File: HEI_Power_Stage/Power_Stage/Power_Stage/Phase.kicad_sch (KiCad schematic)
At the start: 31 parts, among them IC1 ACS730KLCTR-65ABT, Q1 EPC2304ENGRT, Q2 EPC2304ENGRT, U2 MP18831-4AGY

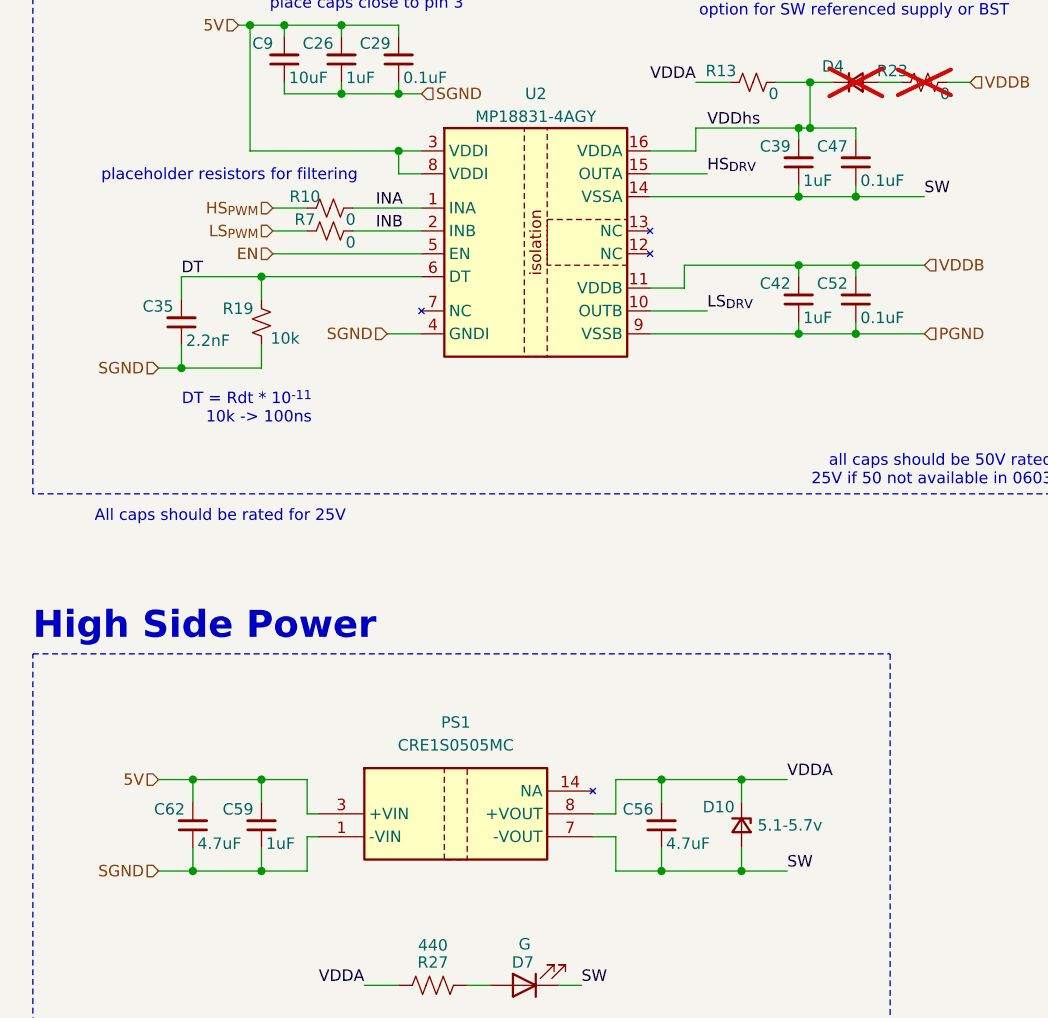
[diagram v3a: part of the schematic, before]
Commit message: placement rough draft
roughly placed all components
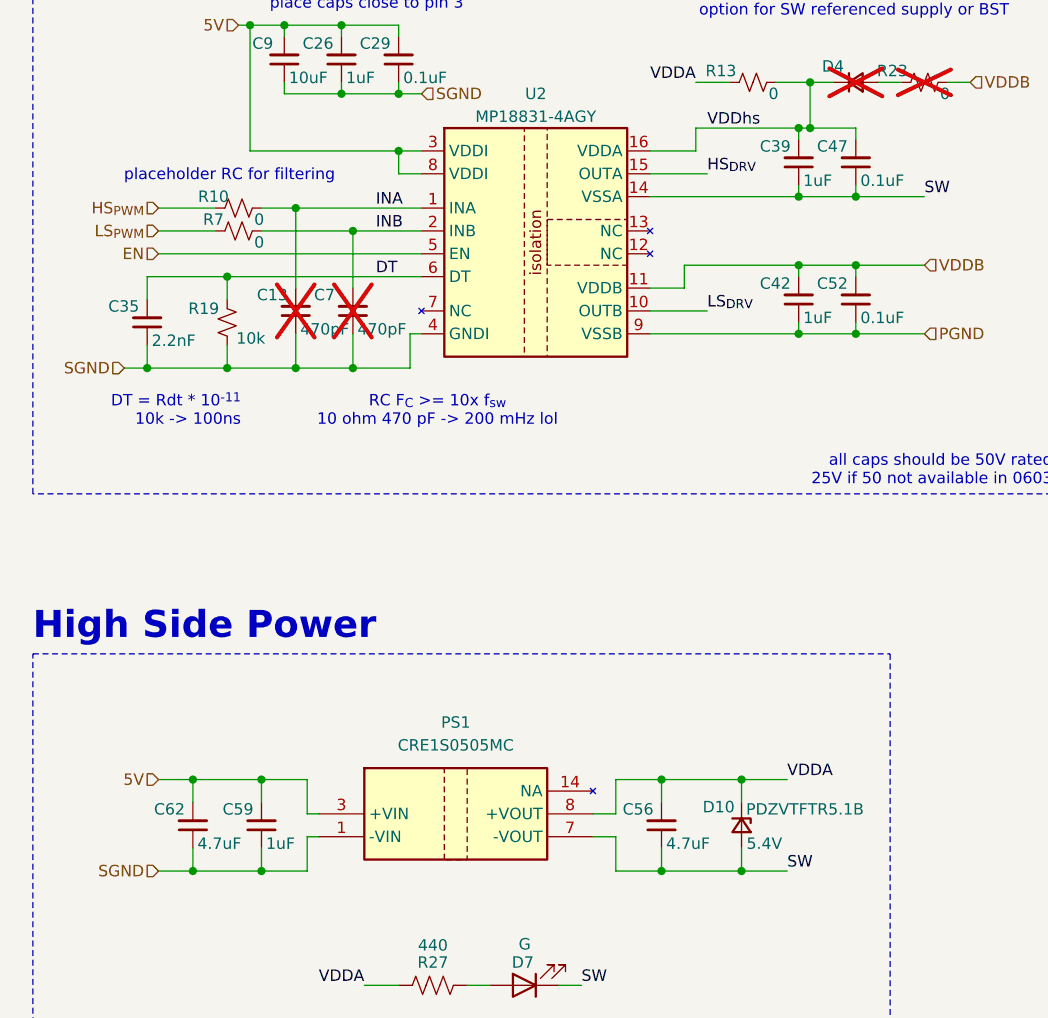
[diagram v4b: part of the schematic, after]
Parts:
- added C13, C7: 470pF, Capacitor_SMD:C_0603_1608Metric_Pad1.08x0.95mm_HandSolder, symbol Device:C_Small
- D10: value 5.1-5.7v -> PDZVTFTR5.1B; Vbreakdown (none) -> 5.4V
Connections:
- net INA: now also C13.2
- net INB: now also C7.2
- net SGND: now also C13.1, C7.1
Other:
- note added: "RC F_{C} >= 10x f_{sw} 10 ohm 470 pF -> 200 mHz lol"
- note added: "placeholder RC for filtering"
- note removed: "All caps should be rated for 25V"
- note removed: "placeholder resistors for filtering"
- moved on the sheet: C35, R10, R19, R7

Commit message: some change
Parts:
- added D13, D22: PDZVTFTR5.1B, Diode_SMD:D_SOD-128, symbol Device:D_Zener_Small
- added D14, D19: 300mV 1A, Diode_SMD:D_SOD-123F, symbol Device:D_Schottky_Small
- added R31, R5: 0, Resistor_SMD:R_0603_1608Metric_Pad0.98x0.95mm_HandSolder, symbol Device:R_Small_US
- D4: value ~ -> 300mV 1A; footprint Diode_SMD:D_SOD-523 -> Diode_SMD:D_SOD-123F; symbol Device:D_Small -> Device:D_Schottky_Small
- R23: footprint LED_SMD:LED_0603_1608Metric_Pad1.05x0.95mm_HandSolder -> Resistor_SMD:R_0603_1608Metric_Pad0.98x0.95mm_HandSolder
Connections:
- net HS_{DRV}: now also R5.1
- net HS_{Gate}: now also D14.2 (A), D22.1 (K)
- net LS_{DRV}: now also R31.1
- net LS_{Gate}: now also D13.1 (K), D19.2 (A)
- net PGND: now also D13.2 (A)
- net SW: now also D22.2 (A)
- new net: D14.1 (K), R5.2
- new net: D19.1 (K), R31.2
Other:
- note added: "zener on output of regulator to limit voltage into VDDx or on output of driver to limit directly into gate"
- moved on the sheet: R14, R4

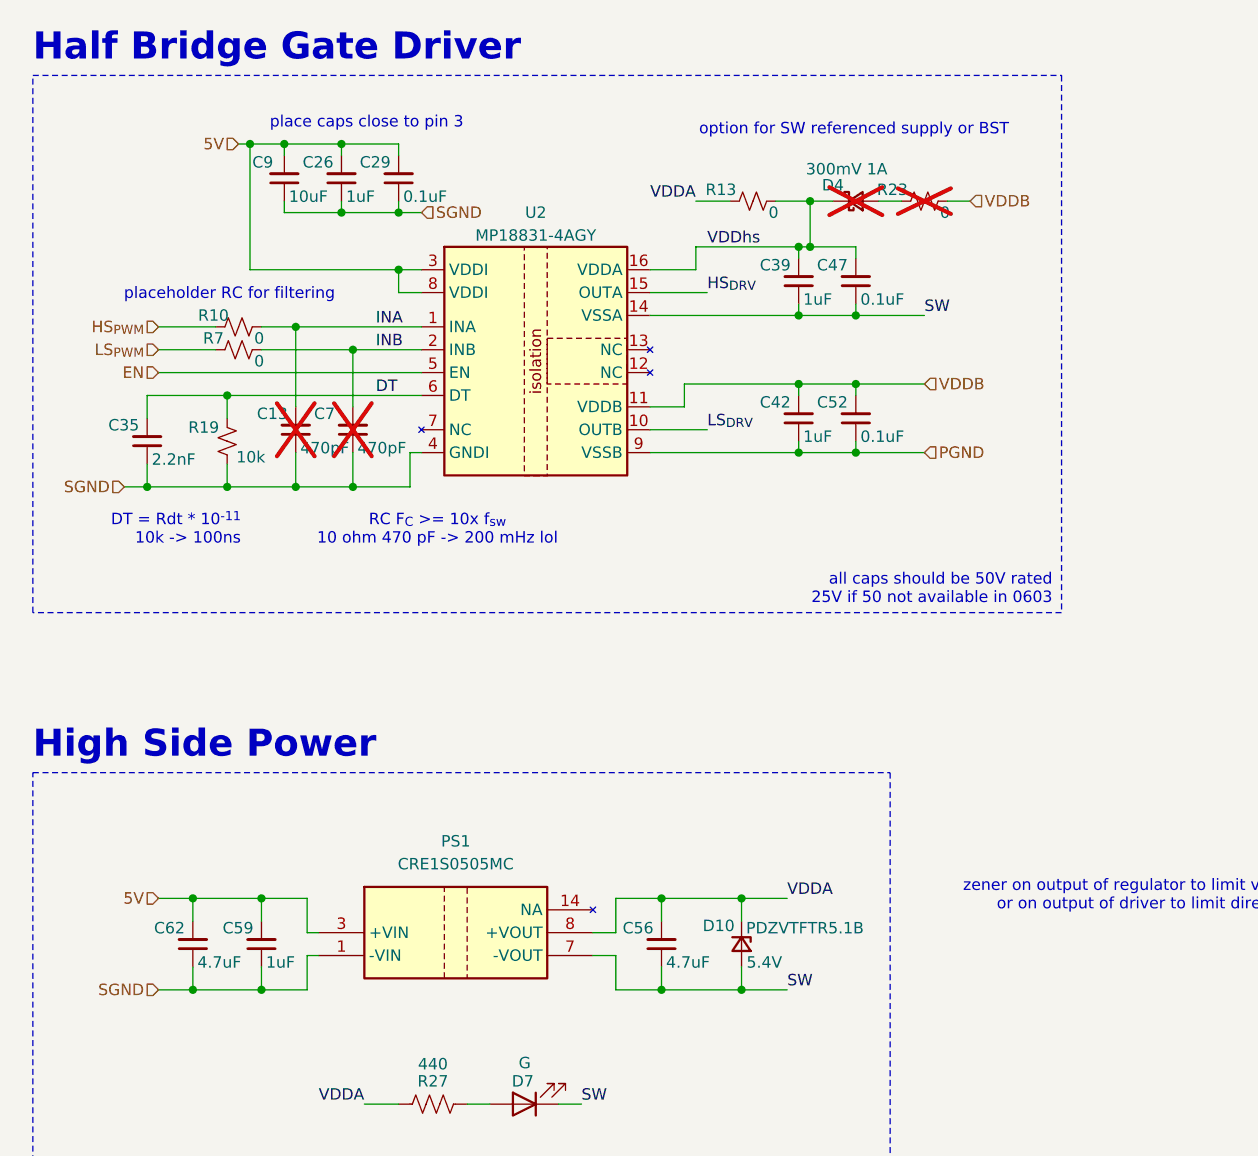
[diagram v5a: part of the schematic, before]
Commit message: all initial placement
initial placement done
routing for one stage done and copied
will make edits and recopy later but wanted to see preview
12.2 x 7.4cm
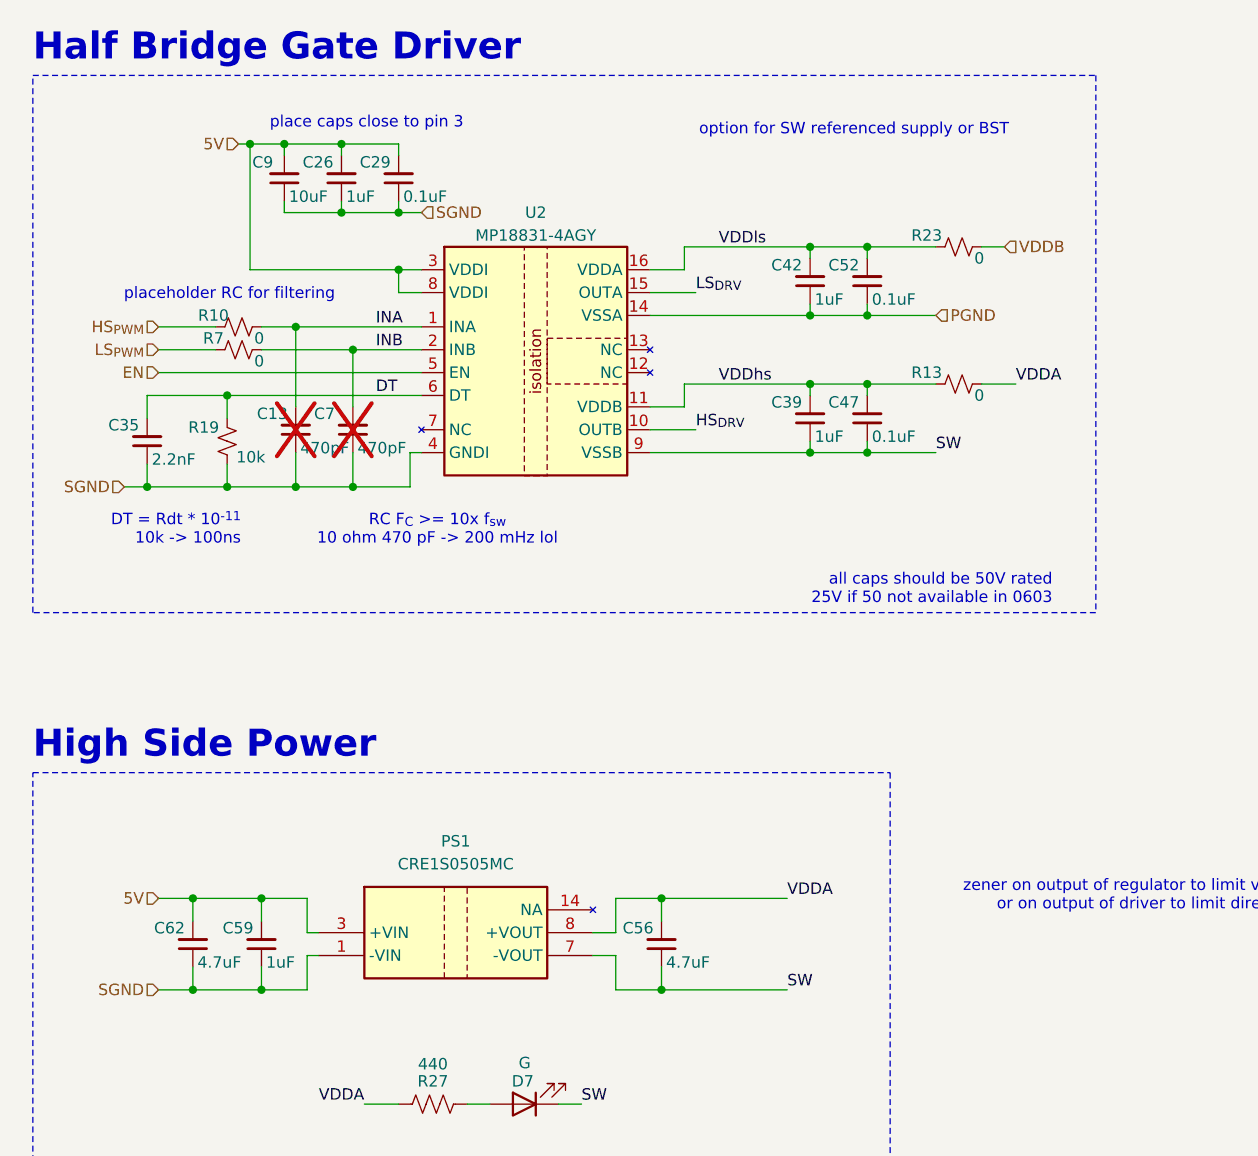
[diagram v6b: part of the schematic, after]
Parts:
- removed D10: PDZVTFTR5.1B, Diode_SMD:D_SOD-128, symbol Device:D_Zener_Small
- removed D4: 300mV 1A, Diode_SMD:D_SOD-123F, symbol Device:D_Schottky_Small
- D13, D22: footprint Diode_SMD:D_SOD-128 -> Diode_SMD:D_SOD-323F
- R23: now fitted
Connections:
- net HS_{DRV}: now also U2.10 (OUTB); no longer U2.15 (OUTA)
- net LS_{DRV}: now also U2.15 (OUTA); no longer U2.10 (OUTB)
- net PGND: now also U2.14 (VSSA); no longer U2.9 (VSSB)
- net SW: now also U2.9 (VSSB); no longer U2.14 (VSSA)
- net VDDA: now also R13.2; no longer R13.1
- net VDDB: no longer C42.2, C52.2, U2.11 (VDDB)
- net VDDhs: now also R13.1, U2.11 (VDDB); no longer R13.2, U2.16 (VDDA)
- net VDDls: now reaches R23.1
- net VDDls: now also C42.2, C52.2, U2.16 (VDDA)
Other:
- moved on the sheet: C39, C42, C47, C52, R13

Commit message: big layout change
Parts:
- removed TP5, TP6: Test_Point, TestPoint:TestPoint_Pad_D1.0mm, symbol GTSR_symbol_lib:Test_Point
- added C31: 0.1uF, Capacitor_SMD:C_0603_1608Metric_Pad1.08x0.95mm_HandSolder, symbol Device:C_Small
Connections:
- net 5V: now also C31.2
- net HS_{PWM}: now also R7.1; no longer R10.1
- net LS_{PWM}: now also R10.1; no longer R7.1
- net SGND: now also C31.1
- net PH_{Isense} renamed PH_{Isense}+
- net PH_{Isense}ref renamed PH_{Isense}-
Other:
- moved on the sheet: C26, C29, C9
